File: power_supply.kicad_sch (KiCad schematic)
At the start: 46 parts

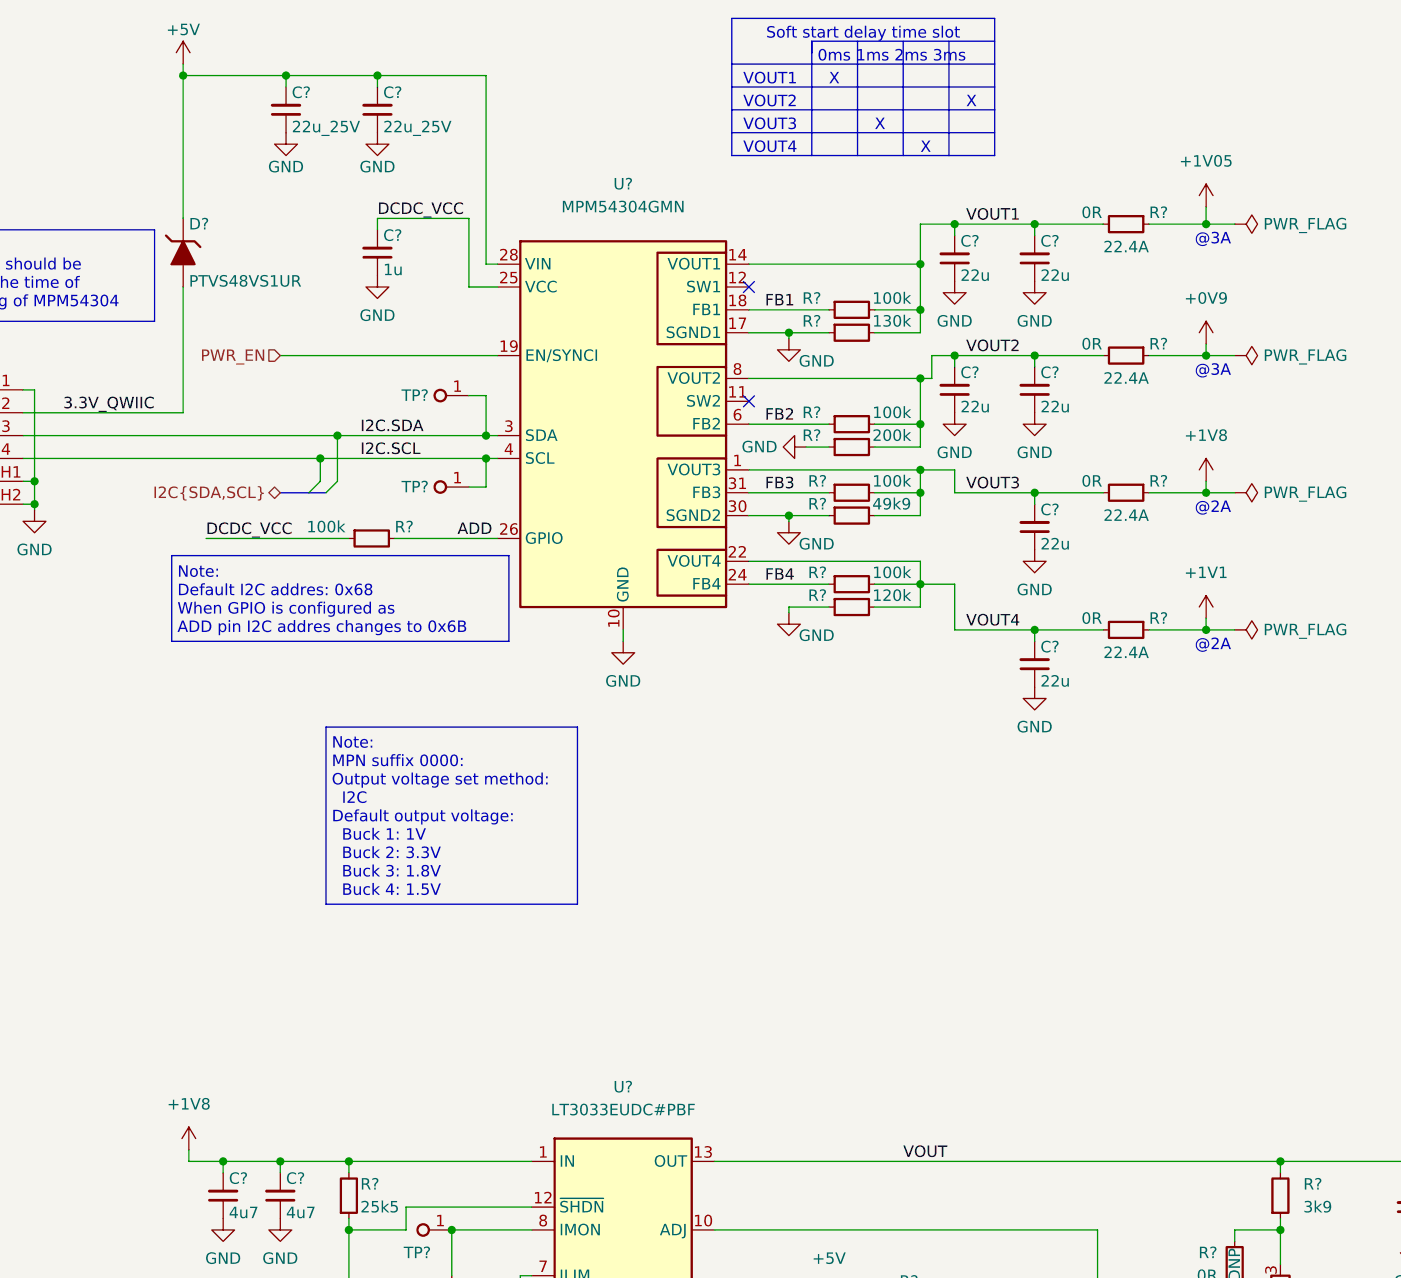
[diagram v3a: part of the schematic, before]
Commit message: [#52536] schematics: adjust outputs based on LPDDR5 voltage ramps
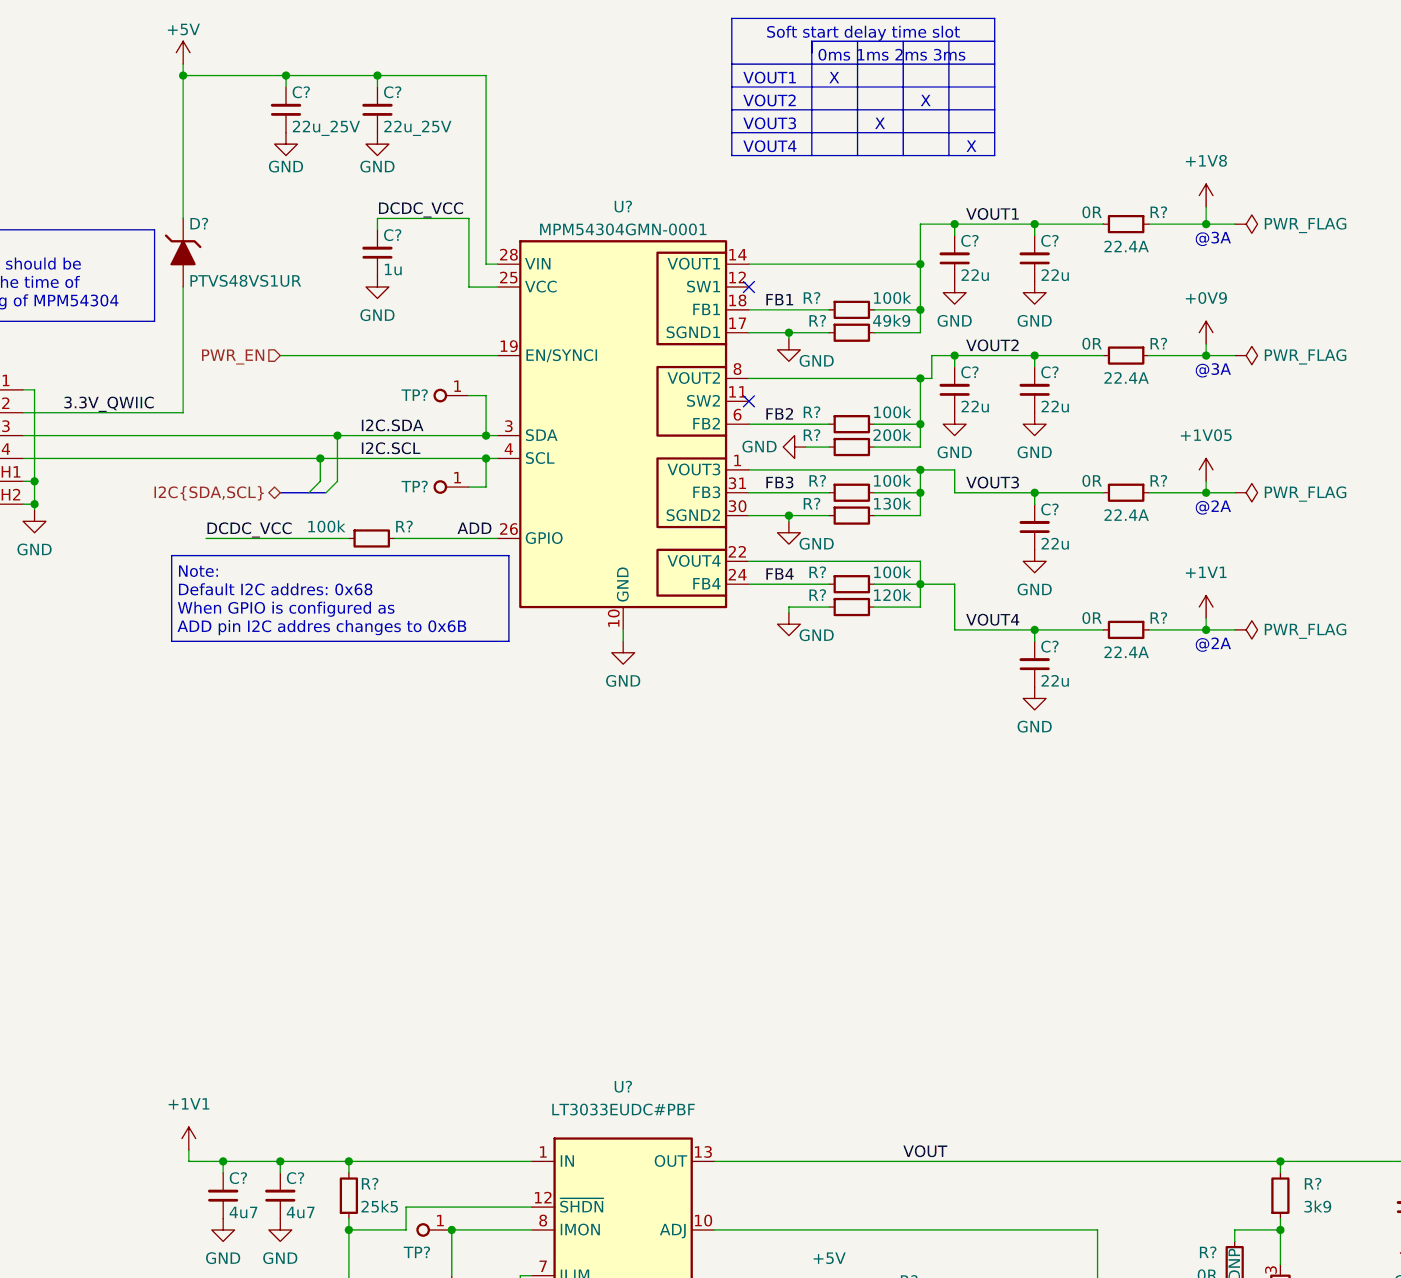
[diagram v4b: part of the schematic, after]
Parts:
- removed U?: MPM54304GMN, antmicro-footprints:MPS_LGA-33, symbol antmicroPMICVoltageRegulatorsDCDCSwitchingRegulators:MPM54304GMN
- added U?: MPM54304GMN-0001, antmicro-footprints:MPS_LGA-33, symbol antmicroPMICVoltageRegulatorsDCDCSwitchingRegulators:MPM54304GMN-0001
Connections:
- net +1V05: now also R?.1; no longer R?.1
- net +1V1: now also C?.2, C?.2, R?.2, U?.1 (IN), U?.15 (IN), U?.16 (IN), U?.2 (IN), U?.21 (IN), U?.22 (IN)
- net +1V8: now also R?.1; no longer C?.2, C?.2, R?.1, R?.2, U?.1 (IN), U?.15 (IN), U?.16 (IN), U?.2 (IN), U?.21 (IN), U?.22 (IN)
- net +5V: now also U?.28 (VIN), U?.29 (VIN)
- net ADD: now also U?.26 (GPIO)
- net DCDC_VCC: now also U?.25 (VCC)
- net FB1: now also U?.18 (FB1)
- net FB2: now also U?.6 (FB2)
- net FB3: now also U?.31 (FB3)
- net FB4: now also U?.24 (FB4)
- net GND: now also U?.10 (GND), U?.13 (GND), U?.16 (GND), U?.17 (SGND1), U?.2 (GND), U?.20 (GND), U?.21 (GND), U?.27 (GND), U?.30 (SGND2), U?.33 (GND), U?.5 (GND), U?.7 (GND)
- net I2C.SCL: now also U?.4 (SCL)
- net I2C.SDA: now also U?.3 (SDA)
- net PWR_EN: now also U?.19 (EN/SYNCI)
- net VOUT1: now also R?.2, U?.14 (VOUT1), U?.15 (VOUT1); no longer R?.2
- net VOUT2: now also U?.8 (VOUT2), U?.9 (VOUT2)
- net VOUT3: now also R?.2, U?.1 (VOUT3), U?.32 (VOUT3); no longer R?.2
- net VOUT4: now also U?.22 (VOUT4), U?.23 (VOUT4)
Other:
- note removed: "Note: MPN suffix 0000: Output voltage set method: I2C Default output voltage: Buck 1: 1V Buck 2: 3.3V Buck 3: 1.8V Buck 4: 1.5V"
- moved on the sheet: R?

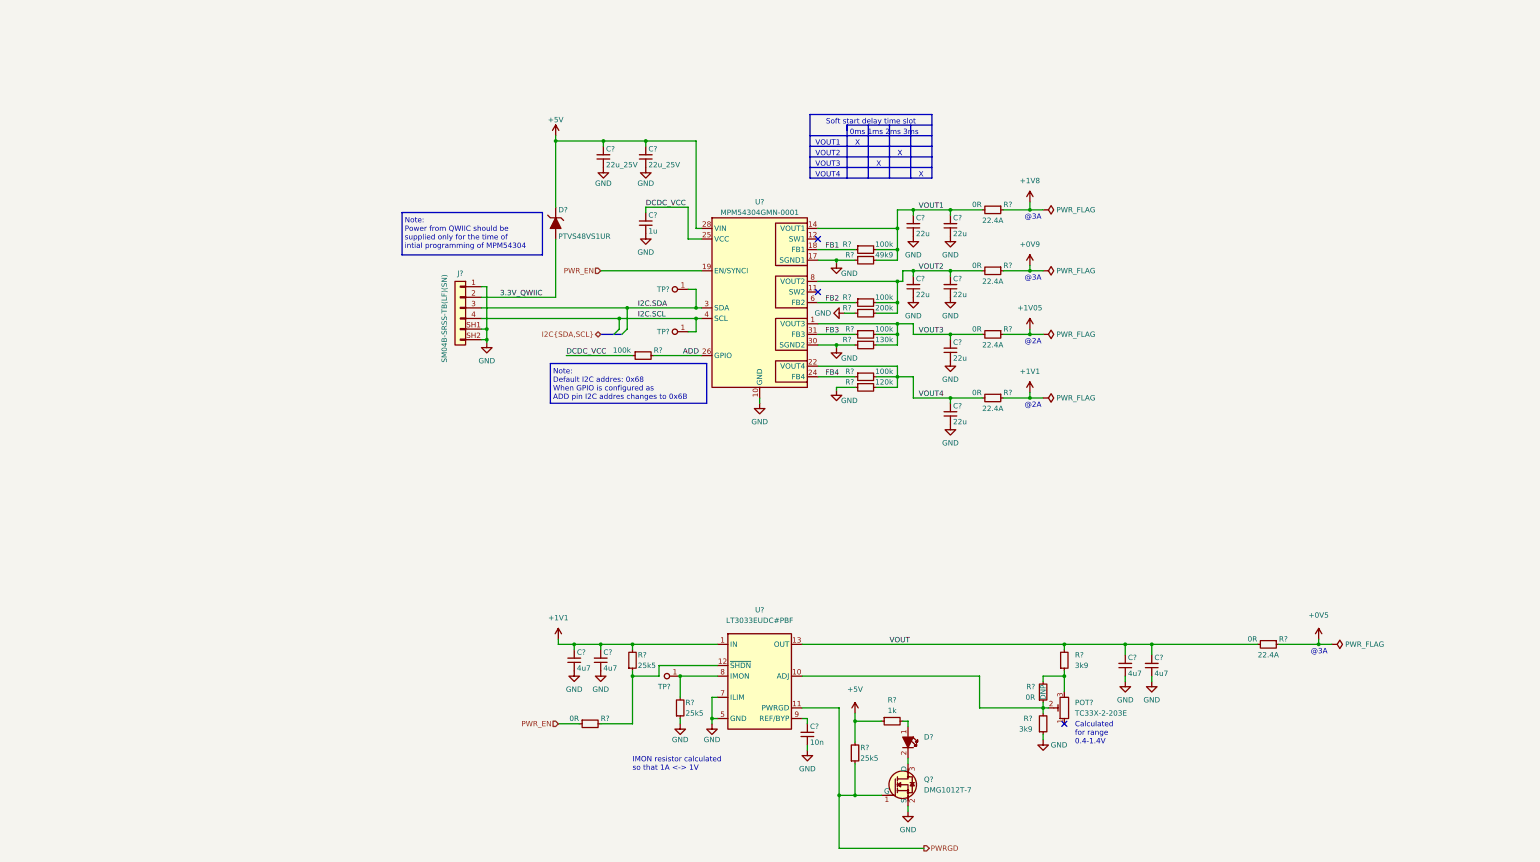
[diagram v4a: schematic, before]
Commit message: [#52835] schematics: update components after standardization
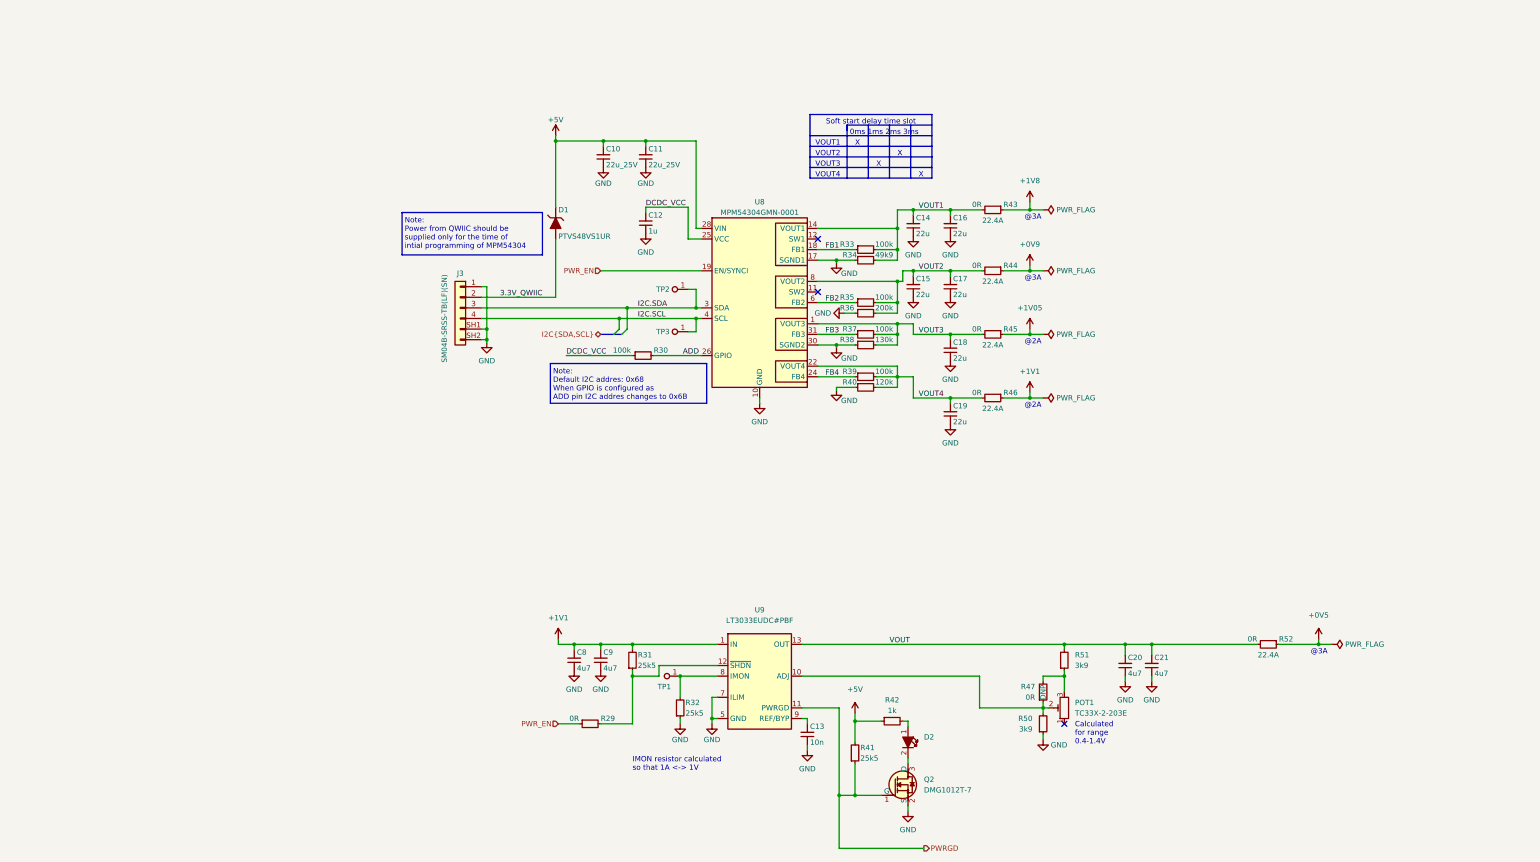
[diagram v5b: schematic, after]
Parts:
- gave numbers to parts that had none: 46
